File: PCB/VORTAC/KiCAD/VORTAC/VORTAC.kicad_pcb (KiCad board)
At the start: 4 copper layers, 46 x 52.4 mm, 114 parts, among them IC1 TMC2209-LA, J1 DEBUG, J10 FAN_01_V, J11 FAN_02_V, J12 LED_V, J13 THERM_R, J14 918-418K2023S40001, J15 STEPPER, J16 IO, J2 Molex Micro Fit 3.0, J3 MillMax_004, J4 MillMax_004, J5 USB_HOST, J6 HOTEND, J7 FAN_01, J8 FAN_02, J9 LED, Q1 Q_PMOS_GSD, Q2 Q_NMOS_GSD, Q3 WSD4066DN, Q4 Q_NMOS_GSD, Q5 WSD4066DN, Q6 Q_PNP_BEC, Q7 Q_NPN_BEC, U1 TLV73333PDBV, U2 STM32F103C8Tx, U3 TPS54335ADRCR, U4 TPS54335ADRCR, U5 ADXL345BCCZ-RL7, U6 TJA1040T

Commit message: Routing WIP
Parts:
- removed JP3, JP4: SolderJumper_2_Open, ToolChanger:SolderJumper_Hex_Open_Pad
- added C36: 0.1uF 16V, Capacitor_SMD:C_0402_1005Metric, F.Cu at (95.8, 104.4)
- added C37: 0.1uF 16V, Capacitor_SMD:C_0402_1005Metric, F.Cu at (86.9, 104.9)
- added C38: 0.1uF 16V, Capacitor_SMD:C_0402_1005Metric, F.Cu at (95.3, 95.5)
- added C39: 0.1uF 16V, Capacitor_SMD:C_0402_1005Metric, F.Cu at (94.8, 104.4)
- added C40: 4.7uF 10V, Capacitor_SMD:C_0402_1005Metric, F.Cu at (95.3, 96.5)
- added C41: 0.1uF 16V, Capacitor_SMD:C_0603_1608Metric, F.Cu at (104.4, 82.0)
- added C42: C_Small, Capacitor_SMD:C_0402_1005Metric, F.Cu at (92.3, 91.6)
- added C43: C_Small, Capacitor_SMD:C_0402_1005Metric, F.Cu at (87.2, 91.6)
- added C44: 10nF, Capacitor_SMD:C_0402_1005Metric, F.Cu at (87.4, 96.0)
- added C45: 1uF, Capacitor_SMD:C_0402_1005Metric, F.Cu at (86.4, 96.0)
- added HSE1: 8MHz, Crystal:Crystal_SMD_3225-4Pin_3.2x2.5mm, F.Cu at (89.8, 92.4)
- added L3: 10uH 15mA, Inductor_SMD:L_0805_2012Metric, F.Cu at (83.6, 128.3)
- added R37: R_Small, Resistor_SMD:R_0402_1005Metric, F.Cu at (86.8, 93.7)
- C1: footprint Resistor_SMD:R_0603_1608Metric -> Capacitor_SMD:C_1206_3216Metric
- C11, C6, C7, C9: value 0.1uF -> 0.1uF 50V
- C2: value 0.1uF -> 0.1uF 16V; footprint Capacitor_SMD:C_0402_1005Metric -> Capacitor_SMD:C_0603_1608Metric
- C31: value 100nF 16V -> 0.1uF 16V
- C33: value 100nF 16V -> 0.1uF 16V; footprint Capacitor_SMD:C_0603_1608Metric -> Capacitor_SMD:C_0402_1005Metric
- C4, C5: value 10uF -> 10uF 50V
- IC1: footprint ToolChanger:tmc_2209_VORTAC -> ToolChanger:tmc_2209_package
- J15: footprint Connector_JST:JST_PH_S4B-PH-K_1x04_P2.00mm_Horizontal -> ToolChanger:JST_PH_S4B-PH-K_1x04_P2.00mm_Horizontal
- JP1: value SolderJumper_2_Bridged -> DATA_H JUMPER; footprint ToolChanger:SolderJumper_Hex_Bridged_Pad -> Jumper:SolderJumper-3_P1.3mm_Bridged12_Pad1.0x1.5mm
- JP2: value SolderJumper_2_Bridged -> DATA_L JUMPER; footprint ToolChanger:SolderJumper_Hex_Bridged_Pad -> Jumper:SolderJumper-3_P1.3mm_Bridged12_Pad1.0x1.5mm
- L1: renamed from 10uH1; value L -> 10uH
- L2: renamed from 10uH2; value L -> 10uH
- moved JP2 53.2 mm to (111.9, 103.3), turned to 180 degrees
- moved JP1 49.3 mm to (111.9, 100.8), turned to 180 degrees
- moved C33 31.4 mm to (86.9, 103.9), turned to 0 degrees
- moved C25 13.4 mm to (94.5, 90.7), turned to 90 degrees
- moved C30 12.8 mm to (105.5, 90.7), turned to 90 degrees
- moved R18 11.1 mm to (107.6, 82.8), turned to 270 degrees
- moved C8 8.90 mm to (83.3, 120.6)
- moved U1 8.90 mm to (83.7, 123.1)
- moved C32 8.05 mm to (85.8, 116.0), turned to 270 degrees
- moved C27 7.97 mm to (98.5, 82.0)
- moved C28 7.58 mm to (101.5, 82.0)
- moved J1 7.50 mm to (80.9, 112.3)
- moved C17 7.31 mm to (101.5, 103.5), turned to 270 degrees
- moved C15 6.85 mm to (106.1, 103.5), turned to 270 degrees
- moved C3 6.49 mm to (81.1, 122.8), turned to 90 degrees
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- renumbered Q3 to Qe
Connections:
- net DOCK_V_IN renamed DOCK_VDC
- net Net-(U2-Pad39) renamed DEBUG_SWO
- net Net-(U2-Pad44) renamed BOOT_0
- net USBH_GATE renamed HOST_USB_GATE
- C1 pad 1: V_IN -> VDC
- C15 pad 1: 12V -> +12V
- C16 pad 1: 5V -> +5V
- C17 pad 1: 12V -> +12V
- C18 pad 1: 5V -> +5V
- C19 pad 1: 12V -> +12V
- C20 pad 1: 5V -> +5V
- C21 pad 1: 3.3V -> +3V3
- C24 pad 2: V_IN -> VDC
- C26 pad 2: V_IN -> VDC
- C29 pad 2: V_IN -> VDC
- C3 pad 1: 5V -> +5V
- C32 pad 1: ADXL_AREF -> +3V3
- C33 pad 2: TMC_BRA -> +3V3
- C34 pad 1: V_IN -> VDC
- C35 pad 1: 3.3V -> +3V3
- C4 pad 1: V_IN -> VDC
- C5 pad 1: V_IN -> VDC
- C6 pad 1: V_IN -> VDC
- C7 pad 1: V_IN -> VDC
- C8 pad 1: 3.3V -> +3V3
- D5 pad 1: 5V -> +5V
- IC1 pad 15: 3.3V -> +3V3
- IC1 pad 22: V_IN -> VDC
- IC1 pad 28: V_IN -> VDC
- J1 pad 1: Net-(J1-Pad1) -> DEBUG_SWCLK
- J1 pad 2: Net-(J1-Pad2) -> DEBUG_SWDIO
- J1 pad 3: Net-(J1-Pad3) -> GND
- J1 pad 4: Net-(J1-Pad4) -> NRST
- J1 pad 5: Net-(J1-Pad5) -> +3V3
- J1 pad 6: Net-(J1-Pad6) -> BOOT_1
- J10 pad 1: V_IN -> FAN_1_V_OUT
- J10 pad 2: FAN_1_V_OUT -> VDC
- J10 pad 3: 12V -> FAN_1_V_OUT
- J10 pad 4: FAN_1_V_OUT -> +12V
- J10 pad 5: 5V -> FAN_1_V_OUT
- J10 pad 6: FAN_1_V_OUT -> +5V
- J11 pad 1: V_IN -> FAN_2_V_OUT
- J11 pad 2: FAN_2_V_OUT -> VDC
- J11 pad 3: 12V -> FAN_2_V_OUT
- J11 pad 4: FAN_2_V_OUT -> +12V
- J11 pad 5: 5V -> FAN_2_V_OUT
- J11 pad 6: FAN_2_V_OUT -> +5V
- J12 pad 1: V_IN -> LED_1_V_OUT
- J12 pad 2: LED_1_V_OUT -> VDC
- J12 pad 3: 12V -> LED_1_V_OUT
- J12 pad 4: LED_1_V_OUT -> +12V
- J12 pad 5: 5V -> LED_1_V_OUT
- J12 pad 6: LED_1_V_OUT -> +5V
- J13 pad 2: AREF -> +3.3VA
- J13 pad 4: AREF -> +3.3VA
- J16 pad 1: 5V -> +5V
- J3 pad 3: V_IN -> VDC
- J5 pad 1: 5V -> +5V
- J5 pad 2: HOST_USB_D+ -> HOST_USB_DRAIN
- J5 pad 3: HOST_USB_D- -> HOST_USB_D+
- J5 pad 4: HOST_USB_DRAIN -> HOST_USB_D-
- J6 pad 2: V_IN -> VDC
- J7 pad 1: FAN_1_DRAIN -> FAN_1_V_OUT
- J7 pad 2: FAN_1_TACHO -> FAN_1_DRAIN
- J7 pad 3: FAN_1_V_OUT -> FAN_1_TACHO
- J8 pad 1: FAN_2_DRAIN -> FAN_2_V_OUT
- J8 pad 2: FAN_2_TACHO -> FAN_2_DRAIN
- J8 pad 3: FAN_2_V_OUT -> FAN_2_TACHO
- J9 pad 1: LED_1_DRAIN -> LED_1_V_OUT
- J9 pad 2: LED_1_V_OUT -> LED_1_DRAIN
- JP1 pad 1: Net-(JP1-Pad1) -> CAN_H
- JP1 pad 2: Net-(JP1-Pad2) -> TOOL_DATA_H
- JP2 pad 1: Net-(JP2-Pad1) -> CAN_L
- JP2 pad 2: Net-(JP2-Pad2) -> TOOL_DATA_L
- L1 pad 2: 12V -> +12V
- L2 pad 2: 5V -> +5V
- Q1 pad 2: V_IN -> VDC
- R26 pad 1: 12V -> +12V
- R28 pad 1: 5V -> +5V
- R32 pad 2: 3.3V -> +3V3
- R5 pad 1: V_IN -> VDC
- U1 pad 1: 5V -> +5V
- U1 pad 3: 5V -> +5V
- U1 pad 5: 3.3V -> +3V3
- U2 pad 1: Net-(U2-Pad1) -> +3V3
- U2 pad 19: Net-(U2-Pad19) -> BOOT_1
- U2 pad 23: Net-(U2-Pad23) -> GND
- U2 pad 24: Net-(U2-Pad24) -> +3V3
- U2 pad 34: Net-(U2-Pad34) -> DEBUG_SWDIO
- U2 pad 35: Net-(U2-Pad35) -> GND
- U2 pad 36: Net-(U2-Pad36) -> +3V3
- U2 pad 37: Net-(U2-Pad37) -> DEBUG_SWCLK
- U2 pad 47: Net-(U2-Pad47) -> GND
- U2 pad 48: Net-(U2-Pad48) -> +3V3
- U2 pad 5: Net-(U2-Pad5) -> HSE_OSC_IN
- U2 pad 6: Net-(U2-Pad6) -> HSE_OSC_OUT
- U2 pad 7: Net-(U2-Pad7) -> NRST
- U2 pad 8: Net-(U2-Pad8) -> GND
- U2 pad 9: Net-(U2-Pad9) -> +3.3VA
- U3 pad 1: V_IN -> VDC
- U4 pad 1: V_IN -> VDC
- U5 pad 1: ADXL_AREF -> +3V3
- U5 pad 6: ADXL_AREF -> +3V3
- U6 pad 3: 3.3V -> +3V3
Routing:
- net GND: track 0.00 -> 33.5 mm, vias 0 -> 36
- net FAN_1_TACHO: track 0.00 -> 21.3 mm
- net FAN_2_TACHO: track 0.00 -> 10.1 mm
- net +3V3: track 0.00 -> 9.24 mm
- net LED_1_DRAIN: track 0.00 -> 9.11 mm
- net FAN_2_DRAIN: track 0.00 -> 8.47 mm
- net VDC: track 0.00 -> 7.50 mm, vias 0 -> 22
- net TOOL_ID: track 0.00 -> 7.26 mm
- net TOOL_DATA_H: track 0.00 -> 6.56 mm
- net FAN_1_DRAIN: track 0.00 -> 6.07 mm
- net Net-(Q7-Pad2): track 0.00 -> 5.02 mm
- net Net-(Q6-Pad2): track 0.00 -> 4.97 mm
- net Net-(D4-Pad1): track 0.00 -> 4.50 mm
- net TMC_STEP: track 0.00 -> 4.12 mm
- net Net-(D1-Pad1): track 0.00 -> 4.04 mm
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- added copper zone on In2.Cu, net +12V
- added copper zone on In2.Cu, net +5V
- added copper zone on F.Cu, net DOCK_GND
- added copper zone on In1.Cu, net DOCK_GND
- added copper zone on F.Cu, net DOCK_VDC
- added copper zone on B.Cu, net GND
- added copper zone on F.Cu, net GND
- added copper zone on In1.Cu, net GND
- added copper zone on F.Cu, net HEATER_DRAIN
- added copper zone on F.Cu, net STEP_1_A1
- added copper zone on B.Cu, net STEP_1_A2
- added copper zone on F.Cu, net STEP_1_A2
- added copper zone on F.Cu, net STEP_1_B1
- added copper zone on B.Cu, net STEP_1_B2
- added copper zone on F.Cu, net STEP_1_B2
- added copper zone on F.Cu, net TMC_BRA
- added copper zone on F.Cu, net TMC_BRB
- added copper zone on F.Cu, net VDC
- added copper zone on In2.Cu, net VDC
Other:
- outline, holes or cut-outs redrawn
- net class Default: clearance 0.2 -> 0.15
- net class Wide added: clearance 0.2, trace_width 0.5, via_dia 1.2, via_drill 0.6
- rule trace_clearance: 0.2 -> 0.15

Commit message: Reversed voltage selectors to simplify routing
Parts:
- J1, J10, J11, J12: footprint Connector_PinHeader_1.27mm:PinHeader_2x03_P1.27mm_Vertical -> ToolChanger:PinHeader_2x03_P1.27mm_Vertical
- J13: footprint Connector_PinHeader_1.27mm:PinHeader_2x02_P1.27mm_Vertical -> ToolChanger:PinHeader_2x02_P1.27mm_Vertical
- moved J12 0.42 mm to (82.6, 93.0)
- moved J11 0.07 mm to (82.6, 88.3)
- renumbered Qe to Q3
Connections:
- J10 pad 1: FAN_1_V_OUT -> VDC
- J10 pad 2: VDC -> FAN_1_V_OUT
- J10 pad 3: FAN_1_V_OUT -> +12V
- J10 pad 4: +12V -> FAN_1_V_OUT
- J10 pad 5: FAN_1_V_OUT -> +5V
- J10 pad 6: +5V -> FAN_1_V_OUT
- J11 pad 1: FAN_2_V_OUT -> VDC
- J11 pad 2: VDC -> FAN_2_V_OUT
- J11 pad 3: FAN_2_V_OUT -> +12V
- J11 pad 4: +12V -> FAN_2_V_OUT
- J11 pad 5: FAN_2_V_OUT -> +5V
- J11 pad 6: +5V -> FAN_2_V_OUT
- J12 pad 1: LED_1_V_OUT -> VDC
- J12 pad 2: VDC -> LED_1_V_OUT
- J12 pad 3: LED_1_V_OUT -> +12V
- J12 pad 4: +12V -> LED_1_V_OUT
- J12 pad 5: LED_1_V_OUT -> +5V
- J12 pad 6: +5V -> LED_1_V_OUT
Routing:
- net FAN_1_V_OUT: track 3.25 -> 0.00 mm

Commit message: More Routing
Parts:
- added D6: LED_Small, LED_SMD:LED_0402_1005Metric, F.Cu at (84.8, 102.4)
- added D7: NeoPixel_THT, LED_SMD:LED_Cree-PLCC4_2x2mm_CW, F.Cu at (100.0, 95.3)
- added D8: SK6812, LED_SMD:LED_SK6812_PLCC4_5.0x5.0mm_P3.2mm, F.Cu at (112.5, 134.2)
- added R38: R_Small, Resistor_SMD:R_0402_1005Metric, F.Cu at (84.8, 101.5)
- IC1: footprint ToolChanger:tmc_2209_package -> ToolChanger:tmc_2209_ThermalPad
- J9: footprint Connector_JST:JST_PH_B2B-PH-K_1x02_P2.00mm_Vertical -> Connector_JST:JST_PH_B3B-PH-K_1x03_P2.00mm_Vertical
- moved L3 29.4 mm to (84.6, 99.0), turned to 90 degrees
- moved J1 7.74 mm to (87.5, 108.2)
- moved C17 6.67 mm to (100.0, 110.0), turned to 0 degrees
- moved C15 6.57 mm to (100.0, 105.8), turned to 0 degrees
- moved R35 6.10 mm to (104.2, 104.0), turned to 180 degrees
- moved C19 5.86 mm to (100.0, 107.9), turned to 0 degrees
- moved R36 5.34 mm to (104.2, 103.0), turned to 180 degrees
- moved C13 4.26 mm to (93.0, 129.1)
- moved C14 4.26 mm to (101.6, 129.1)
- moved C9 4.26 mm to (97.3, 129.1)
- moved R22 4.26 mm to (95.0, 128.3)
- moved R23 4.26 mm to (103.6, 128.3)
- moved C11 4.26 mm to (105.9, 129.1)
- moved C10 4.14 mm to (93.0, 127.5)
- moved L2 4.12 mm to (105.5, 108.2)
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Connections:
- net ADXL_SDO renamed Net-(U5-Pad12)
- net USART_1_RX renamed Net-(U2-Pad31)
- net USART_1_TX renamed Net-(U2-Pad30)
- J1 pad 1: DEBUG_SWCLK -> BOOT_1
- J1 pad 2: DEBUG_SWDIO -> +3V3
- J1 pad 3: GND -> NRST
- J1 pad 4: NRST -> GND
- J1 pad 5: +3V3 -> DEBUG_SWDIO
- J1 pad 6: BOOT_1 -> DEBUG_SWCLK
- J16 pad 3: IO_1_OUT -> IO_3_OUT
- J16 pad 5: IO_3_OUT -> IO_1_OUT
- J2 pad 1: GND -> DOCK_GND
- J2 pad 2: DOCK_GND -> DOCK_VDC
- J2 pad 3: DOCK_VDC -> GND
- J3 pad 1: TOOL_ID -> GND
- J3 pad 2: Net-(J3-Pad2) -> GND
- J3 pad 4: GND -> TOOL_DATA_H
- J4 pad 1: HOST_USB_D- -> GND
- J4 pad 2: HOST_USB_D+ -> HOST_USB_D-
- J4 pad 3: TOOL_DATA_H -> HOST_USB_D+
- J4 pad 4: TOOL_DATA_L -> TOOL_ID
- U2 pad 10: Net-(U2-Pad10) -> TOOL_ID
- U2 pad 11: Net-(U2-Pad11) -> TMC_ENN
- U2 pad 12: USART_2_TX -> TMC_UART_TX
- U2 pad 13: USART_2_RX -> TMC_UART_RX
- U2 pad 14: Net-(U2-Pad14) -> FAN_1_GATE
- U2 pad 15: Net-(U2-Pad15) -> FAN_2_GATE
- U2 pad 16: Net-(U2-Pad16) -> FAN_2_TACHO
- U2 pad 17: Net-(U2-Pad17) -> FAN_1_TACHO
- U2 pad 18: Net-(U2-Pad18) -> LED_1_PWM
- U2 pad 2: Net-(U2-Pad2) -> TMC_STEP
- U2 pad 20: Net-(U2-Pad20) -> LED_0
- U2 pad 21: USART_3_TX -> ADXL_SCL
- U2 pad 22: USART_3_RX -> ADXL_SDA
- U2 pad 25: Net-(U2-Pad25) -> ADXL_CS
- U2 pad 26: Net-(U2-Pad26) -> ADXL_INT1
- U2 pad 27: Net-(U2-Pad27) -> LED_1_GATE
- U2 pad 28: Net-(U2-Pad28) -> HOST_USB_GATE
- U2 pad 3: Net-(U2-Pad3) -> TMC_DIR
- U2 pad 38: Net-(U2-Pad38) -> THERM_1_PIN
- U2 pad 39: DEBUG_SWO -> IO_3_OUT
- U2 pad 4: Net-(U2-Pad4) -> TMC_DIAG
- U2 pad 40: Net-(U2-Pad40) -> IO_2_OUT
- U2 pad 41: Net-(U2-Pad41) -> IO_1_OUT
- U2 pad 42: Net-(U2-Pad42) -> HEATER_GATE
- U5 pad 13: ADXL_SDI -> ADXL_SDA
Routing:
- net TOOL_ID: track 7.26 -> 45.8 mm
- net HOST_USB_D+: track 0.00 -> 28.8 mm
- net HOST_USB_D-: track 0.00 -> 23.0 mm
- net TOOL_DATA_L: track 3.32 -> 20.8 mm
- net TOOL_DATA_H: track 6.56 -> 23.9 mm
- net FAN_2_GATE: track 0.00 -> 17.1 mm
- net DOCK_GND: track 2.20 -> 18.3 mm, vias 12 -> 24
- net Net-(D3-Pad2): track 1.21 -> 16.4 mm, vias 0 -> 2
- net FAN_1_GATE: track 0.00 -> 14.8 mm
- net +5V: track 0.00 -> 14.5 mm, vias 0 -> 3
- net VDC: track 7.50 -> 21.2 mm, vias 22 -> 23
- net GND: track 33.5 -> 44.8 mm, vias 36 -> 39
- net DOCK_VDC: track 2.22 -> 12.5 mm, vias 12 -> 23
- net LED_1_PWM: track 0.00 -> 9.70 mm
- net FAN_1_V_OUT: track 0.00 -> 8.78 mm
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- added copper zone on B.Cu, net DOCK_GND
- added copper zone on B.Cu, net DOCK_VDC
- added copper zone on B.Cu, net HEATER_DRAIN
- removed copper zone on In1.Cu, net DOCK_GND
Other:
- net class 0.35mm added: clearance 0.2, trace_width 0.35, via_dia 0.8, via_drill 0.4
- net class 0.5mm added: clearance 0.2, trace_width 0.5, via_dia 1.2, via_drill 0.6
- net class 2.0mm added: clearance 0.2, trace_width 2, via_dia 0.8, via_drill 0.4
- net class Wide removed

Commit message: Still Routing
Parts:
- Q1, Q2, Q4: footprint ToolChanger:IRF9310PbF-1_SO-8 -> ToolChanger:IRF9310PbF-1_SO-8_ThermalPad
- moved C43 10.8 mm to (84.0, 101.5), turned to 180 degrees
- moved C42 10.1 mm to (85.5, 97.9)
- moved HSE1 9.91 mm to (83.4, 99.0), turned to 270 degrees
- moved C36 9.71 mm to (95.5, 94.1), turned to 180 degrees
- moved D6 9.59 mm to (94.0, 105.1), turned to 270 degrees
- moved C37 9.04 mm to (96.0, 103.0), turned to 90 degrees
- moved R38 8.98 mm to (93.0, 105.1), turned to 90 degrees
- moved C38 8.86 mm to (86.6, 94.6), turned to 270 degrees
- moved C39 8.72 mm to (95.5, 95.1), turned to 180 degrees
- moved L3 8.34 mm to (90.5, 104.8), turned to 180 degrees
- moved C45 8.12 mm to (87.0, 103.5), turned to 180 degrees
- moved C40 7.98 mm to (87.6, 94.6), turned to 270 degrees
- moved C33 7.96 mm to (95.0, 103.0), turned to 90 degrees
- moved D7 7.81 mm to (105.6, 100.8)
- moved R37 7.23 mm to (85.5, 100.1), turned to 90 degrees
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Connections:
- C42 pad 2: GND -> GND1
- C43 pad 2: GND -> GND1
- HSE1 pad 2: GND -> GND1
- HSE1 pad 4: GND -> GND1
- U2 pad 10: TOOL_ID -> Net-(U2-Pad10)
- U2 pad 11: TMC_ENN -> Net-(U2-Pad11)
- U2 pad 12: TMC_UART_TX -> Net-(U2-Pad12)
- U2 pad 13: TMC_UART_RX -> Net-(U2-Pad13)
- U2 pad 14: FAN_1_GATE -> Net-(U2-Pad14)
- U2 pad 15: FAN_2_GATE -> Net-(U2-Pad15)
- U2 pad 16: FAN_2_TACHO -> Net-(U2-Pad16)
- U2 pad 17: FAN_1_TACHO -> Net-(U2-Pad17)
- U2 pad 18: LED_1_PWM -> Net-(U2-Pad18)
- U2 pad 19: BOOT_1 -> Net-(U2-Pad19)
- U2 pad 2: TMC_STEP -> Net-(U2-Pad2)
- U2 pad 20: LED_0 -> Net-(U2-Pad20)
- U2 pad 25: ADXL_CS -> Net-(U2-Pad25)
- U2 pad 26: ADXL_INT1 -> Net-(U2-Pad26)
- U2 pad 27: LED_1_GATE -> Net-(U2-Pad27)
- U2 pad 28: HOST_USB_GATE -> Net-(U2-Pad28)
- U2 pad 3: TMC_DIR -> Net-(U2-Pad3)
- U2 pad 38: THERM_1_PIN -> Net-(U2-Pad38)
- U2 pad 39: IO_3_OUT -> Net-(U2-Pad39)
- U2 pad 4: TMC_DIAG -> Net-(U2-Pad4)
- U2 pad 40: IO_2_OUT -> Net-(U2-Pad40)
- U2 pad 41: IO_1_OUT -> Net-(U2-Pad41)
- U2 pad 42: HEATER_GATE -> Net-(U2-Pad42)
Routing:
- net TOOL_ID: track 45.8 -> 69.0 mm
- net TOOL_DATA_H: track 23.9 -> 36.7 mm
- net TOOL_DATA_L: track 20.8 -> 32.8 mm
- net Net-(C9-Pad1): track 0.00 -> 10.6 mm, vias 0 -> 2
- net Net-(C11-Pad1): track 0.00 -> 10.4 mm, vias 0 -> 2
- net Net-(C10-Pad1): track 0.00 -> 7.52 mm
- net Net-(C12-Pad1): track 0.00 -> 7.42 mm
- net GND1: track 0.00 -> 7.22 mm, vias 0 -> 1
- net Net-(C9-Pad2): track 0.00 -> 5.79 mm
- net Net-(C11-Pad2): track 0.00 -> 5.75 mm
- net HSE_OSC_IN: track 0.00 -> 5.57 mm
- net FAN_1_GATE: track 14.8 -> 9.86 mm
- net FAN_2_GATE: track 17.1 -> 12.6 mm
- net LED_1_DRAIN: track 11.0 -> 6.42 mm
- net Net-(C43-Pad1): track 0.00 -> 2.87 mm
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- added copper zone on F.Cu, net +12V
- added copper zone on In2.Cu, net +3V3
- added copper zone on F.Cu, net +5V
- added copper zone on In1.Cu, net GND1
- added copper zone on F.Cu, net Net-(C11-Pad1)
- added copper zone on F.Cu, net Net-(C9-Pad1)
- removed copper zone on B.Cu, net DOCK_GND
- removed copper zone on F.Cu, net DOCK_GND
- removed copper zone on B.Cu, net DOCK_VDC
- removed copper zone on F.Cu, net DOCK_VDC
- removed copper zone on B.Cu, net HEATER_DRAIN
- removed copper zone on F.Cu, net HEATER_DRAIN
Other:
- net class 0.35mm removed

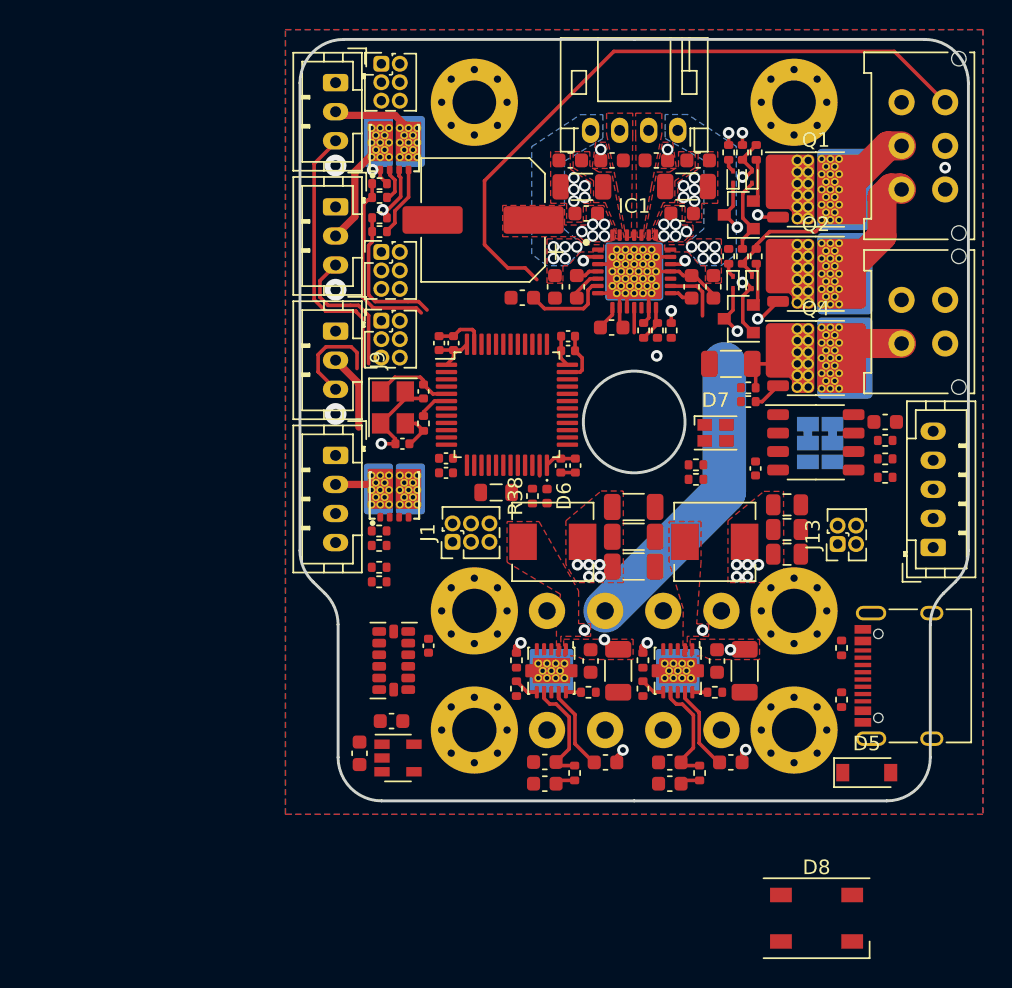
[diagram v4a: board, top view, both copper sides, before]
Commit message: Added Protective Passives
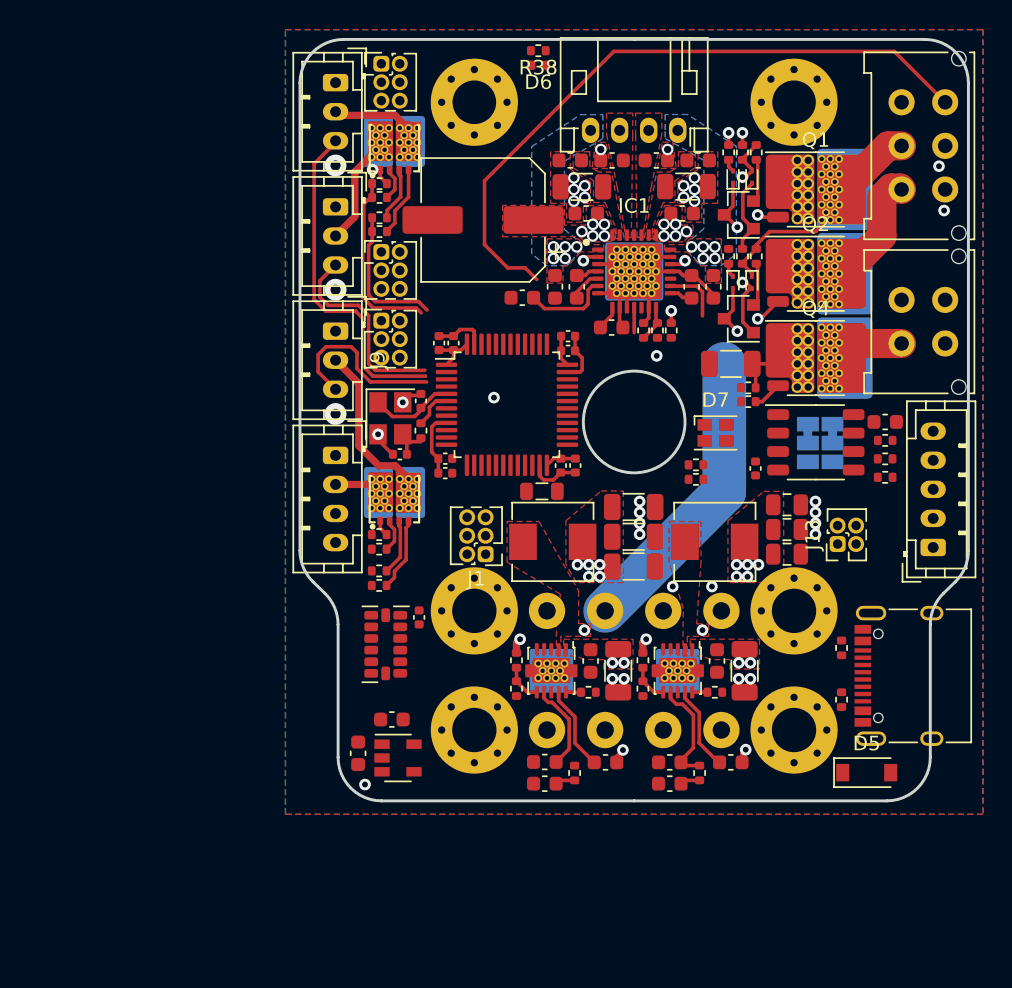
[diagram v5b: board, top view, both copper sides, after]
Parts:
- removed D8: SK6812, LED_SMD:LED_SK6812_PLCC4_5.0x5.0mm_P3.2mm
- moved R38 30.7 mm to (93.4, 74.5), turned to 180 degrees
- moved D6 29.7 mm to (93.4, 75.5), turned to 180 degrees
- moved L3 3.15 mm to (93.7, 104.8)
- moved J1 2.43 mm to (89.8, 109.1), turned to 180 degrees
- moved C32 2.05 mm to (85.2, 113.5)
- moved U5 1.25 mm to (82.9, 115.3)
- moved C44 1.02 mm to (87.0, 103.5), turned to 0 degrees
- moved C45 0.98 mm to (87.0, 102.5), turned to 0 degrees
- moved HSE1 0.77 mm to (83.2, 99.8)
- moved C43 0.75 mm to (83.9, 102.2)
- moved C42 0.67 mm to (85.3, 98.5), turned to 90 degrees
- moved R37 0.53 mm to (85.3, 100.6)
- moved Q3 0.25 mm to (83.5, 105.4)
- moved R12 0.25 mm to (82.5, 107.8)
- moved R13 0.25 mm to (82.5, 110.2)
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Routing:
- net VDC: track 23.8 -> 37.6 mm, vias 13 -> 15
- net GND: track 44.2 -> 51.7 mm, vias 15 -> 30
- net LED_1_DRAIN: track 6.42 -> 12.1 mm
- net LED_1_PWM: track 7.04 -> 12.2 mm
- net Net-(Q3-Pad4): track 0.00 -> 5.07 mm
- net FAN_1_TACHO: track 18.7 -> 23.3 mm
- net +3.3VA: track 0.00 -> 4.50 mm
- net TOOL_DATA_H: track 36.7 -> 32.3 mm
- net FAN_2_TACHO: track 9.85 -> 13.9 mm
- net TOOL_DATA_L: track 32.8 -> 28.8 mm
- net GND1: track 7.22 -> 3.67 mm, vias 1 -> 2
- net Net-(Q3-Pad2): track 0.00 -> 2.31 mm
- net Net-(C10-Pad1): track 7.52 -> 6.05 mm
- net Net-(R26-Pad2): track 1.71 -> 2.64 mm
- net Net-(R28-Pad2): track 1.71 -> 2.64 mm
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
